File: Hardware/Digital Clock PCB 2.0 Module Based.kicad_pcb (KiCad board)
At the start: 2 copper layers, 124.5 x 46 mm, 77 parts, among them J1 USB_C_Receptacle_USB2.0, J2 Conn_01x04, J3 Conn_01x04, Q1 C15127, Q2 C8545, SW1 SW_Push, SW2 SW_Push, U1 ESP32-S2-SOLO-2, U10 SBC18-11SURKCGKWA, U2 AMS1117-3.3, U3 74LS47, U4 74LS47, U5 SBC18-11SURKCGKWA, U6 SBC18-11SURKCGKWA, U7 74LS47, U8 74LS47, U9 SBC18-11SURKCGKWA

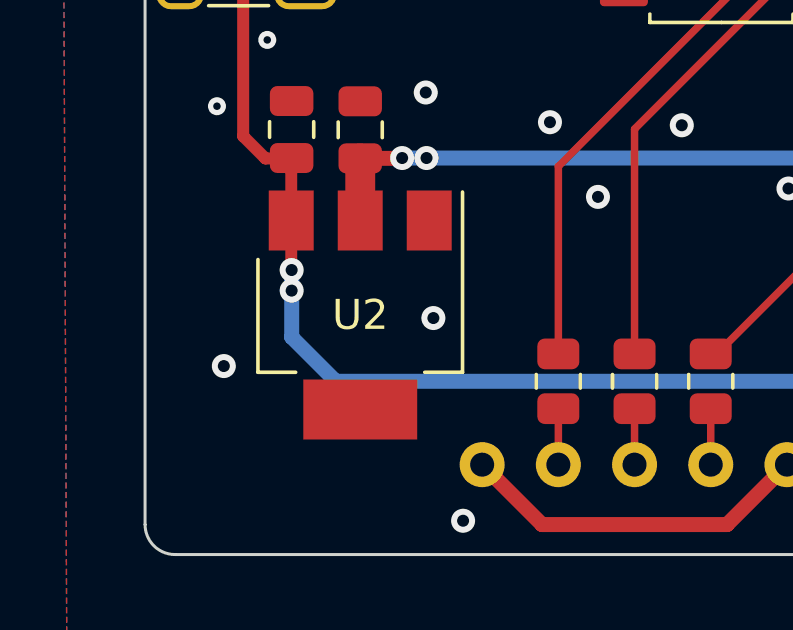
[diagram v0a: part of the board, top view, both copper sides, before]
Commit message: Updates to layout, keep production files off github
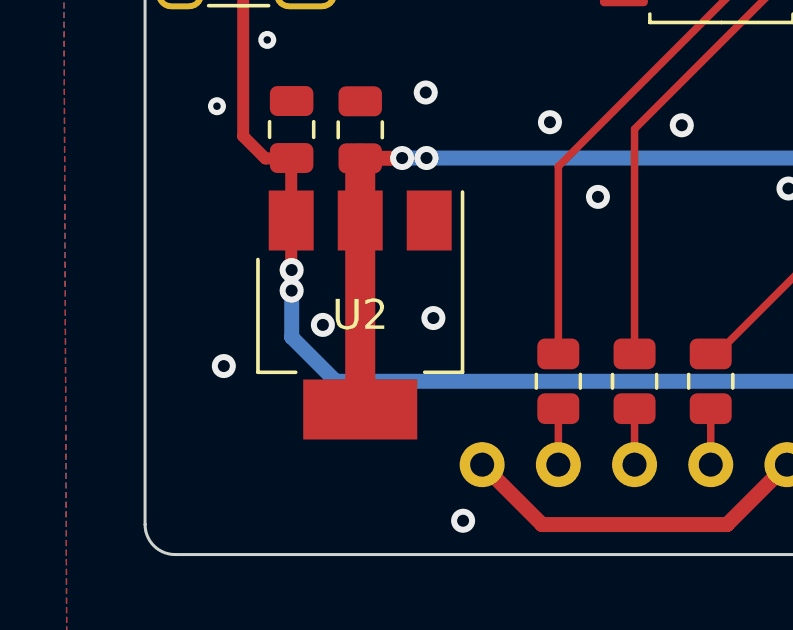
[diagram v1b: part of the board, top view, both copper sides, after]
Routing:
- net +3V3: track 281.5 -> 287.8 mm
- net GND: vias 190 -> 191
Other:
- board text added: "JLCJLCJLCJLC"
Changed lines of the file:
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@@
 			(at -6.0706 -0.9918 180)
 			(layer "F.Fab")
+			(hide yes)
 			(effects
 				(font
@@
 		(layer "Edge.Cuts")
 	)
+	(gr_text "JLCJLCJLCJLC"
+		(at 176.784 119.6848 0)
+		(layer "B.SilkS")
+		(effects
+			(font
+				(size 1 1)
+				(thickness 0.15)
+			)
+			(justify left bottom mirror)
+		)
+	)
 	(gr_text "TX"
 		(at 254.9144 114.8842 0)
@@
 	)
 	(via
+		(at 151.7142 118.6688)
+		(size 0.8)
+		(drill 0.4)
+		(layers "F.Cu" "B.Cu")
+		(free yes)
+		(net 2)
+	)
+	(via
 		(at 175.133 87.0458)
 		(size 0.6)
@@
 		(layer "F.Cu")
 		(net 4)
+	)
+	(segment
+		(start 152.9588 115.1886)
+		(end 152.9588 121.4886)
+		(width 1)
+		(layer "F.Cu")
+		(net 4)
